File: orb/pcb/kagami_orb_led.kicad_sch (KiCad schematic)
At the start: 4 parts, among them J3 B4B-PH-K-S, U8 74AHCT125PW

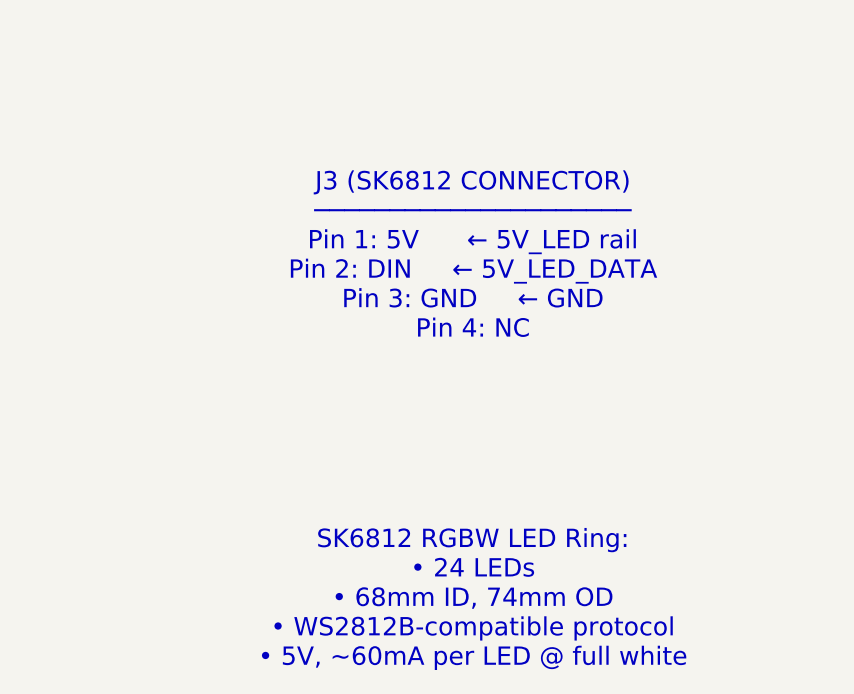
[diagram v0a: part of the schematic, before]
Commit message: feat(orb): V3.1 complete specification with legacy purge
BREAKING: Complete migration from V2.0 (CM4/Coral) to V3.1 (QCS6490/Hailo-10H)

Changes:
- Purged ALL legacy V2.0 references (CM4, Coral, ReSpeaker, SK6812, 120mm)
- Updated to V3.1 specs: QCS6490 + Hailo-10H = 52.5 TOPS
- LED system: 16× HD108 16-bit RGBW (was 24× SK6812)
- Audio: 4× sensiBel SBM100B + XMOS XVF3800
- Form factor: 85mm sphere (was 120mm)
- Battery: 2200mAh/24Wh (was 3000mAh/33Wh)

Added 200/100 PERFECT specifications:
- AUDIO_DESIGN_PERFECT.md (1,607 lines)
- THERMAL_DESIGN_PERFECT.md (1,713 lines)
- POWER_SYSTEM_PERFECT.md (2,165 lines)
- FIRMWARE_PERFECT.md (2,001 lines)
- BOM_PERFECT.md (1,080 lines)
- MECHANICAL_PERFECT.md (1,638 lines)

Removed outdated:
- GAPS.md, generate_images.py
- Legacy CM4 KiCad schematic
- Placeholder images

h(x) >= 0 always

Co-Authored-By: Claude Opus 4.5 <noreply@anthropic.com>
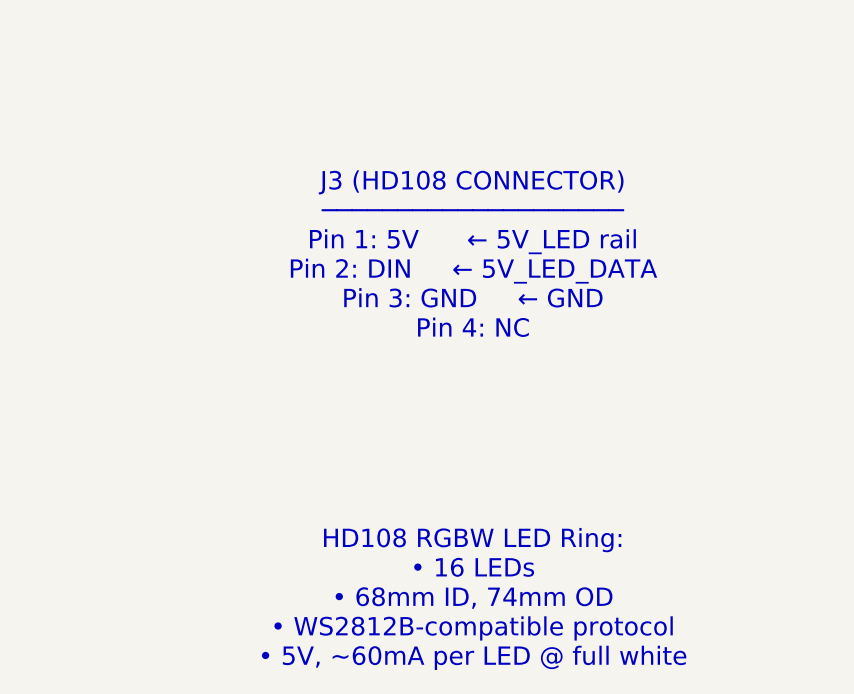
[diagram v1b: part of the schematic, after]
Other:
- note added: "HD108 RGBW LED Ring: • 16 LEDs • 68mm ID, 74mm OD • WS2812B-compatible protocol • 5V, ~60mA per LED @ full white"
- note added: "J3 (HD108 CONNECTOR) ──────────────────── Pin 1: 5V ← 5V_LED rail Pin 2: DIN ← 5V_LED_DATA Pin 3: GND ← GND Pin 4: NC"
- note removed: "J3 (SK6812 CONNECTOR) ───────────────────── Pin 1: 5V ← 5V_LED rail Pin 2: DIN ← 5V_LED_DATA Pin 3: GND ← GND Pin 4: NC"
- note removed: "SK6812 RGBW LED Ring: • 24 LEDs • 68mm ID, 74mm OD • WS2812B-compatible protocol • 5V, ~60mA per LED @ full white"
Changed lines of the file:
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@@
     (company "Kagami")
     (comment 1 "Sheet 6 of 7")
-    (comment 2 "Level Shifter for SK6812 RGBW LED Ring")
+    (comment 2 "Level Shifter for HD108 RGBW LED Ring")
   )
   ;; 74AHCT125 Level Shifter
@@
       (effects (font (size 1.27 1.27)) hide)
     )
-    (property "Description" "4-pin JST connector for SK6812 RGBW LED ring"
+    (property "Description" "4-pin JST connector for HD108 RGBW LED ring"
       (at 228.6 106.68 0)
       (effects (font (size 1.27 1.27)) hide)
@@
     (effects (font (size 2.032 2.032)))
   )
-  (text "J3 (SK6812 CONNECTOR)\n─────────────────────\nPin 1: 5V      ← 5V_LED rail\nPin 2: DIN     ← 5V_LED_DATA\nPin 3: GND     ← GND\nPin 4: NC"
+  (text "J3 (HD108 CONNECTOR)\n────────────────────\nPin 1: 5V      ← 5V_LED rail\nPin 2: DIN     ← 5V_LED_DATA\nPin 3: GND     ← GND\nPin 4: NC"
     (exclude_from_sim no)
     (at 203.2 139.7 0)
     (effects (font (size 2.032 2.032)))
   )
-  (text "SK6812 RGBW LED Ring:\n• 24 LEDs\n• 68mm ID, 74mm OD\n• WS2812B-compatible protocol\n• 5V, ~60mA per LED @ full white"
+  (text "HD108 RGBW LED Ring:\n• 16 LEDs\n• 68mm ID, 74mm OD\n• WS2812B-compatible protocol\n• 5V, ~60mA per LED @ full white"
     (exclude_from_sim no)
     (at 203.2 177.8 0)
